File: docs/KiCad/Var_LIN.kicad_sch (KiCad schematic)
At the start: 28 parts, among them J3 Conn_01x04_Pin, J4 Conn_01x04_Pin, U4 TGS_2611-E00, U5 TLIN2029ADRBRQ1, U6 LMR50410, U7 ATtiny412-SS, U8 BTS4142N

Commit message: Исправление эл.схемы
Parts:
- removed D8: BAV70, Package_TO_SOT_SMD:SOT-23, symbol Diode:BAV70
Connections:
- net OUT1 is gone; now on net OUT: J4.4 (Pin_4)
- net OUT2 is gone; now on net LIN: J4.3 (Pin_3)
- net +5v: now also J3.2 (Pin_2)
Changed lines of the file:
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@@
 	)
 	(junction
-		(at 252.73 50.8)
-		(diameter 0)
-		(color 0 0 0 0)
-	)
-	(junction
 		(at 111.76 142.24)
 		(diameter 0)
@@
 	(wire
 		(pts
-			(xy 238.76 50.8) (xy 242.57 50.8)
-		)
-		(stroke
-			(width 0)
-			(type default)
-		)
-	)
-	(wire
-		(pts
 			(xy 231.14 115.57) (xy 231.14 135.89)
 		)
@@
 	(wire
 		(pts
-			(xy 252.73 50.8) (xy 273.05 50.8)
+			(xy 262.89 50.8) (xy 273.05 50.8)
 		)
 		(stroke
@@
 	(wire
 		(pts
-			(xy 247.65 58.42) (xy 252.73 58.42)
-		)
-		(stroke
-			(width 0)
-			(type default)
-		)
-	)
-	(wire
-		(pts
 			(xy 64.77 139.7) (xy 54.61 139.7)
 		)
@@
 	(wire
 		(pts
-			(xy 247.65 43.18) (xy 252.73 43.18)
-		)
-		(stroke
-			(width 0)
-			(type default)
-		)
-	)
-	(wire
-		(pts
 			(xy 179.07 133.35) (xy 182.88 133.35)
 		)
@@
 	(wire
 		(pts
-			(xy 252.73 58.42) (xy 252.73 50.8)
-		)
-		(stroke
-			(width 0)
-			(type default)
-		)
-	)
-	(wire
-		(pts
 			(xy 170.18 57.15) (xy 175.26 57.15)
 		)
@@
 	(wire
 		(pts
-			(xy 252.73 43.18) (xy 252.73 50.8)
-		)
-		(stroke
-			(width 0)
-			(type default)
-		)
-	)
-	(wire
-		(pts
 			(xy 81.28 132.08) (xy 92.71 132.08)
 		)
@@
 		)
 	)
-	(label "OUT2"
+	(label "LIN"
 		(at 262.89 68.58 180)
 		(effects
@@
 	)
 	(label "+5v"
-		(at 238.76 50.8 180)
+		(at 262.89 50.8 180)
 		(effects
 			(font
@@
 		)
 	)
-	(label "OUT1"
+	(label "OUT"
 		(at 262.89 66.04 180)
 		(effects
@@
 					(unit 1)
 				)
-			)
-		)
-	)
-	(symbol
-		(lib_id "Diode:BAV70")
-		(at 247.65 50.8 270)
-		(unit 1)
-		(body_style 1)
-		(exclude_from_sim no)
-		(in_bom yes)
-		(on_board yes)
-		(in_pos_files yes)
-		(dnp no)
-		(property "Reference" "D8"
-			(at 245.618 41.402 90)
-			(show_name no)
-			(do_not_autoplace no)
-			(effects
-				(font
-					(size 1.27 1.27)
-				)
-				(justify left)
-			)
-		)
-		(property "Value" "BAV70"
-			(at 249.682 41.402 90)
-			(show_name no)
-			(do_not_autoplace no)
-			(effects
-				(font
-					(size 1.27 1.27)
-				)
-				(justify left)
-			)
-		)
-		(property "Footprint" "Package_TO_SOT_SMD:SOT-23"
-			(at 247.65 50.8 0)
-			(hide yes)
-			(show_name no)
-			(do_not_autoplace no)
-			(effects
-				(font
-					(size 1.27 1.27)
-				)
-			)
-		)
-		(property "Datasheet" "https://assets.nexperia.com/documents/data-sheet/BAV70_SER.pdf"
-			(at 247.65 50.8 0)
-			(hide yes)
-			(show_name no)
-			(do_not_autoplace no)
-			(effects
-				(font
-					(size 1.27 1.27)
-				)
-			)
-		)
-		(property "Description" "Dual 100V 215mA high-speed switching diodes, common cathode, SOT-23"
-			(at 247.65 50.8 0)
-			(hide yes)
-			(show_name no)
-			(do_not_autoplace no)
-			(effects
-				(font
-					(size 1.27 1.27)
-				)
-			)
-		)
-		(pin "2"
-		)
-		(pin "1"
-		)
-		(pin "3"
-		)
-		(instances
-			(project "Датчик утечки газа 2026"
-				(path "/a17a5c65-2c8f-4811-931f-2f1634edc76c/5b8447ab-854c-4557-a5fd-39e271aa8951"
-					(reference "D8")
-					(unit 1)
-				)

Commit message: Корректировать номиналы схемы питания. Uвых=4,7v
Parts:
- R21: value 88k -> 82k
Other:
- note added: "4,7В"
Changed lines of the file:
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@@
+		)
+	)
+	(text "4,7В"
+		(exclude_from_sim no)
+		(at 147.828 120.904 0)
+		(effects
+			(font
+				(size 1.27 1.27)
+			)
 		)
 	)
@@
 			)
 		)
-		(property "Value" "88k"
+		(property "Value" "82k"
 			(at 140.208 127.508 0)
 			(show_name no)

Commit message: Разделить платы разных версий
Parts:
- removed D4: BAV70, Package_TO_SOT_SMD:SOT-23, symbol Diode:BAV70
- added D8: MBRA360, Diode_SMD:D_SMA, symbol Device:D
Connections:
- net +24V: now also D8.2 (A); no longer U8.4 (Vbb)
- net +24_V: now reaches R17.2
- net +24_V: now also U8.4 (Vbb), D8.1 (K)
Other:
- moved on the sheet: J3, J4

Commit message: Исправление разводки платы Ver_LIN
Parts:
- R17: footprint Resistor_SMD:R_1210_3225Metric_Pad1.30x2.65mm_HandSolder -> Resistor_SMD:R_1206_3216Metric
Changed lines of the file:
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@@
 			)
 		)
-		(property "Footprint" "Resistor_SMD:R_1210_3225Metric_Pad1.30x2.65mm_HandSolder"
+		(property "Footprint" "Resistor_SMD:R_1206_3216Metric"
 			(at 74.93 130.302 90)
 			(hide yes)

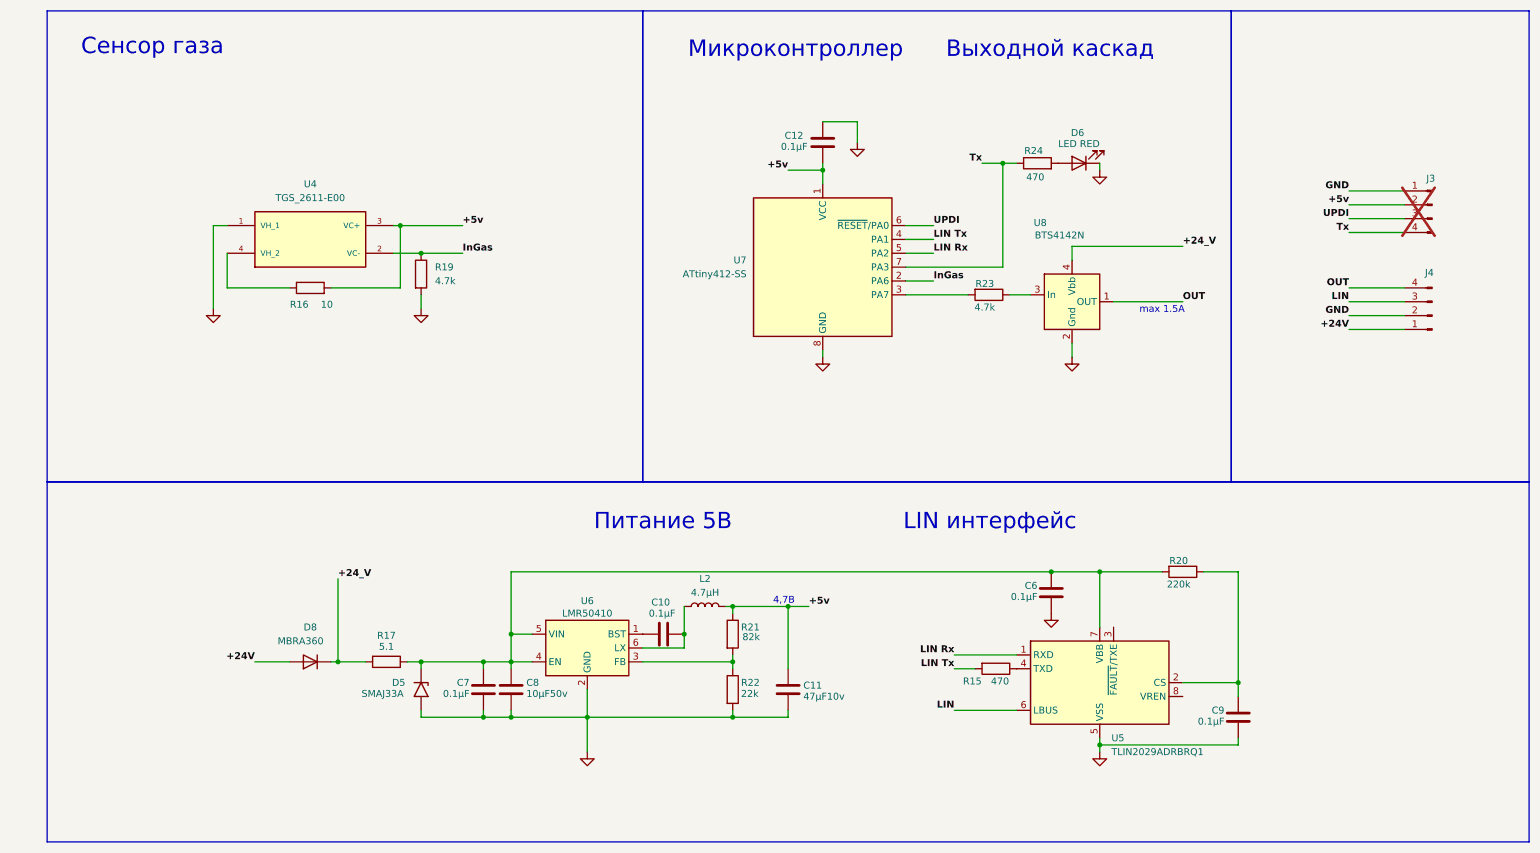
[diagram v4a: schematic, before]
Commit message: Изменить выходной ключ на умный. Правки печатной платы
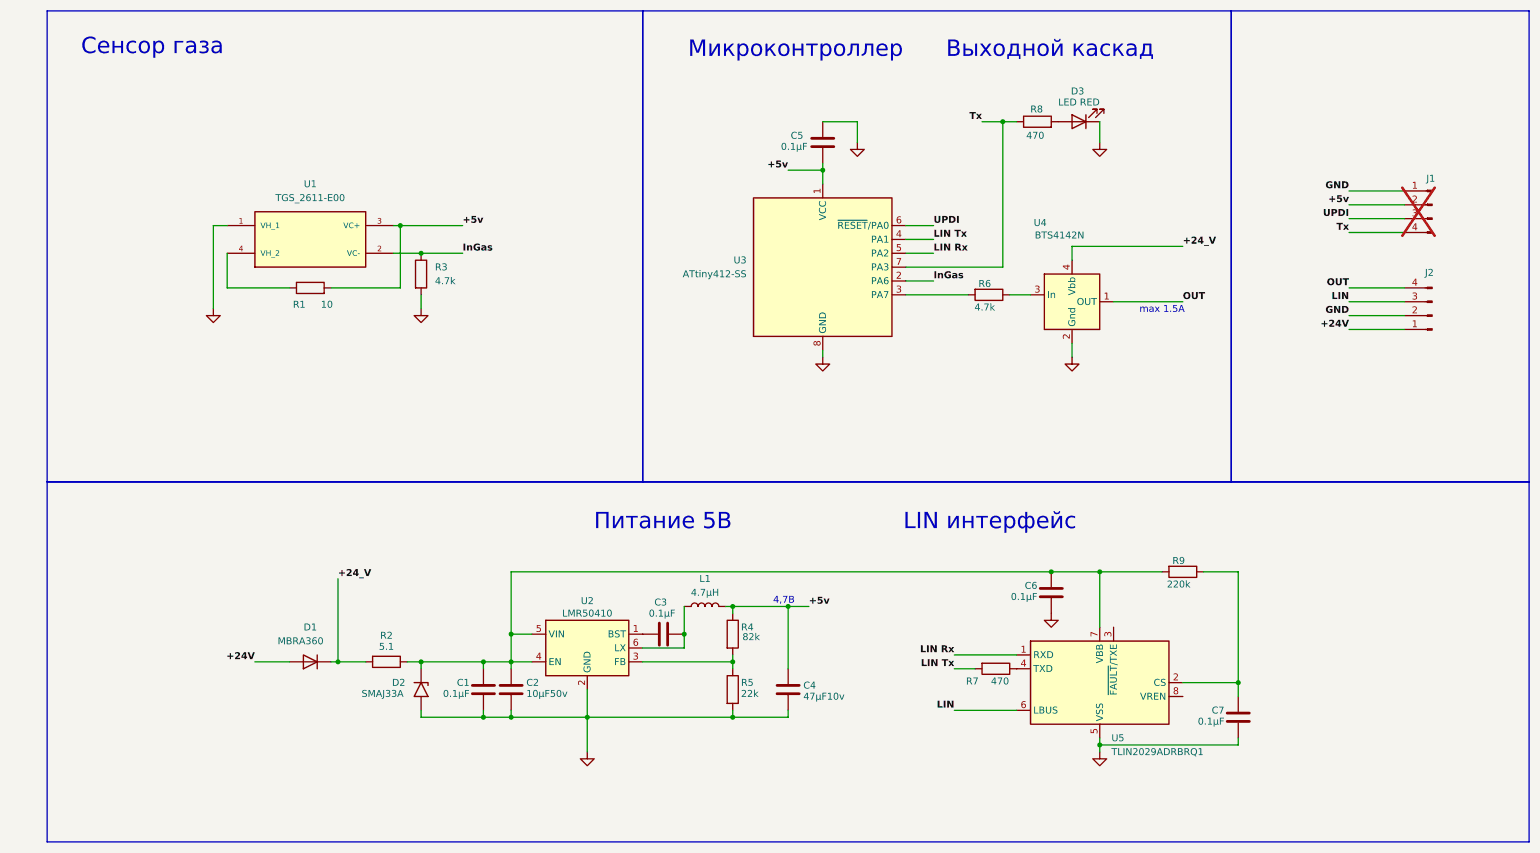
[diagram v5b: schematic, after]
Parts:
- J2: renamed from J4; footprint Connector_Pin:AMP SEAL 3.00mm_4p -> Connector_DIN:SSEAL_4
- U1: renamed from U4; footprint Sensor:TO180P920X780-4P -> Sensor_Humidity:TO180P920X780-4P
- renumbered C7 to C1, C8 to C2, C10 to C3, C11 to C4, C12 to C5, C9 to C7, D8 to D1, D5 to D2, D6 to D3, J3 to J1, L2 to L1, R16 to R1, R17 to R2, R19 to R3, R21 to R4, R22 to R5, R23 to R6, R15 to R7, R24 to R8, R20 to R9, U6 to U2, U7 to U3, U8 to U4
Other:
- moved on the sheet: D3, R8

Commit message: Коррекция ПП. Замена выходной ключ на BTS72002
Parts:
- R2: footprint Resistor_SMD:R_1206_3216Metric -> Resistor_SMD:R_0805_2012Metric
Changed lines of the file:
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@@
 			)
 		)
-		(property "Footprint" "Resistor_SMD:R_1206_3216Metric"
+		(property "Footprint" "Resistor_SMD:R_0805_2012Metric"
 			(at 74.93 130.302 90)
 			(hide yes)

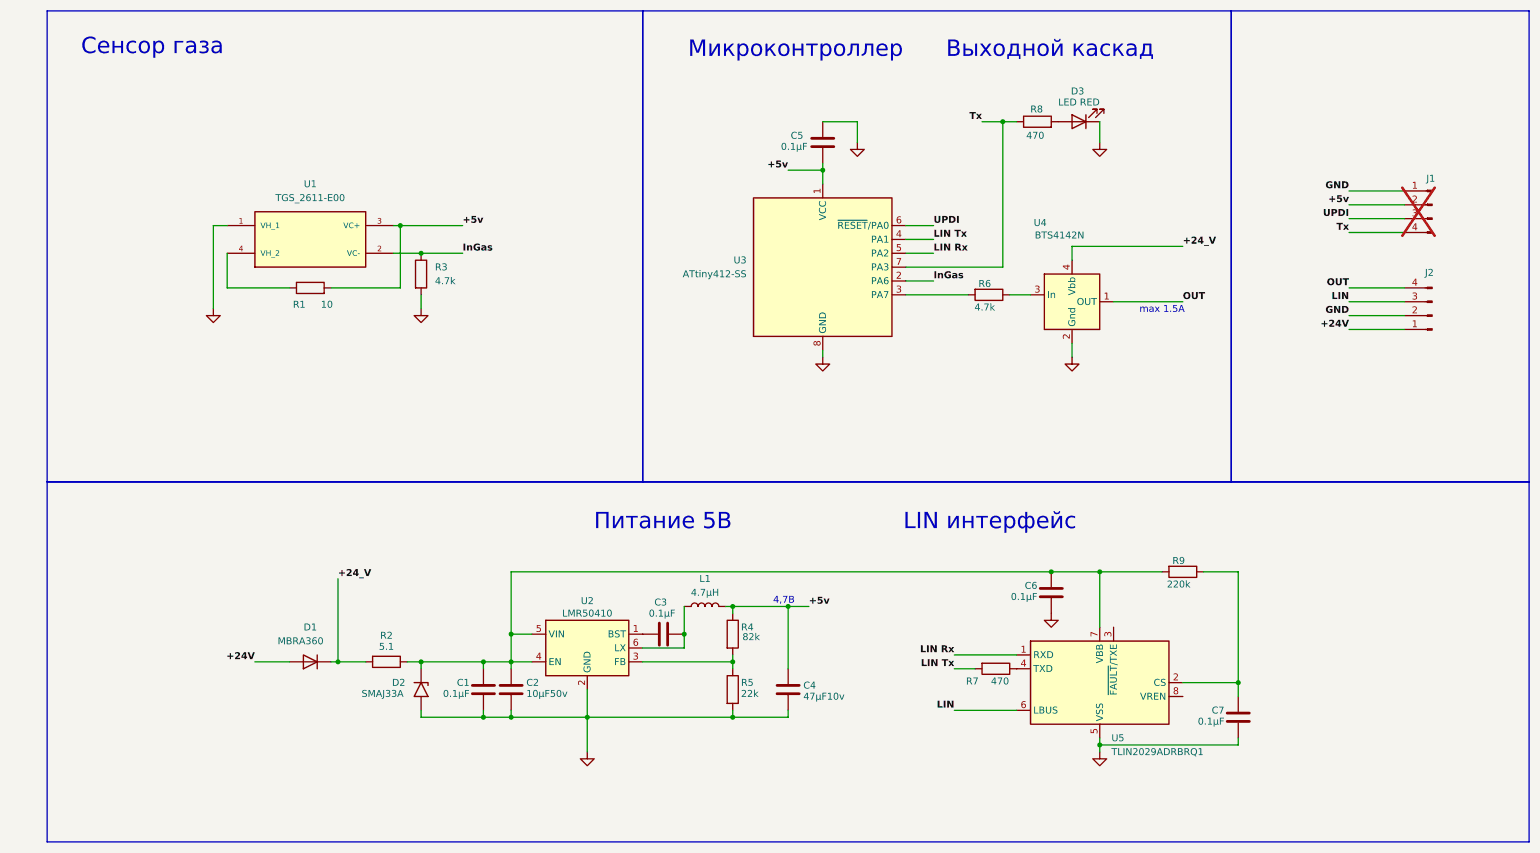
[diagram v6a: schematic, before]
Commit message: Обновить схемы и логику выходного ключа
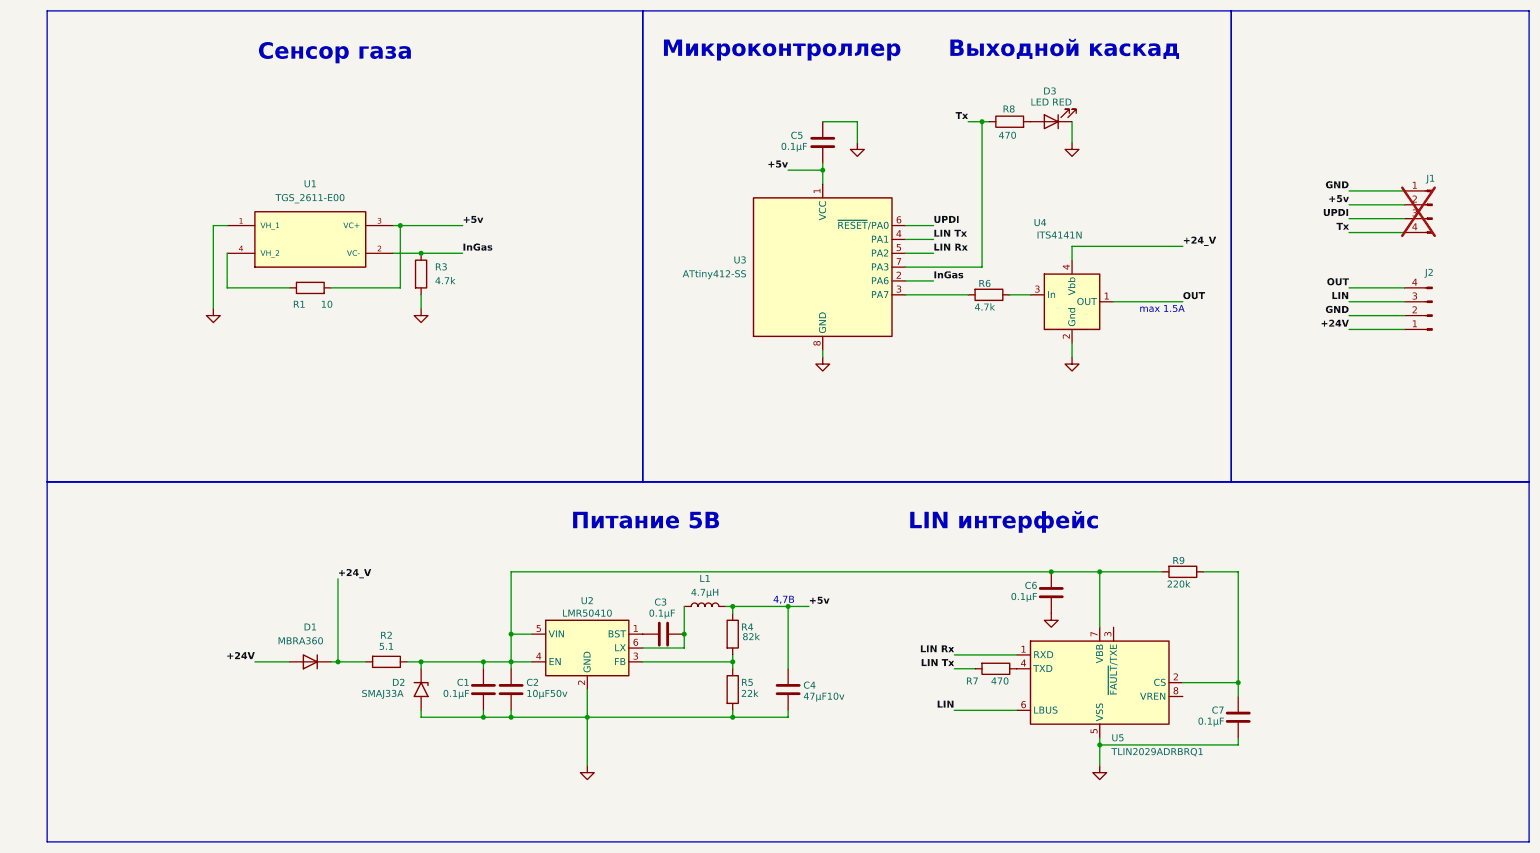
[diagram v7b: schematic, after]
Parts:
- U4: value BTS4142N -> ITS4141N
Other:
- moved on the sheet: D3, R8
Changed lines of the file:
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@@
 	(text "Сенсор газа"
 		(exclude_from_sim no)
-		(at 32.004 19.304 0)
+		(at 65.532 20.32 0)
 		(effects
 			(font
 				(size 3 3)
+				(thickness 0.6)
+				(bold yes)
 			)
 		)
@@
 			(font
 				(size 3 3)
+				(thickness 0.6)
+				(bold yes)
 			)
 		)
@@
 			(font
 				(size 3 3)
+				(thickness 0.6)
+				(bold yes)
 			)
 		)
@@
 	)
 	(junction
-		(at 205.74 147.32)
-		(diameter 0)
-		(color 0 0 0 0)
-	)
-	(junction
 		(at 97.79 142.24)
 		(diameter 0)
@@
 	)
 	(junction
-		(at 187.96 33.02)
-		(diameter 0)
-		(color 0 0 0 0)
-	)
-	(junction
 		(at 154.94 41.91)
 		(diameter 0)
@@
 	)
 	(junction
+		(at 184.15 33.02)
+		(diameter 0)
+		(color 0 0 0 0)
+	)
+	(junction
 		(at 66.04 132.08)
 		(diameter 0)
@@
 	)
 	(junction
+		(at 205.74 147.32)
+		(diameter 0)
+		(color 0 0 0 0)
+	)
+	(junction
 		(at 129.54 127)
 		(diameter 0)
@@
 	(wire
 		(pts
-			(xy 205.74 147.32) (xy 205.74 148.59)
+			(xy 205.74 147.32) (xy 205.74 151.13)
 		)
 		(stroke
@@
 	(wire
 		(pts
-			(xy 187.96 33.02) (xy 190.5 33.02)
-		)
-		(stroke
-			(width 0)
-			(type default)
-		)
-	)
-	(wire
-		(pts
 			(xy 148.59 140.97) (xy 148.59 142.24)
 		)
@@
 	(wire
 		(pts
-			(xy 111.76 148.59) (xy 111.76 142.24)
+			(xy 111.76 151.13) (xy 111.76 142.24)
 		)
 		(stroke
@@
 	(wire
 		(pts
+			(xy 184.15 33.02) (xy 185.42 33.02)
+		)
+		(stroke
+			(width 0)
+			(type default)
+		)
+	)
+	(wire
+		(pts
 			(xy 148.59 133.35) (xy 148.59 121.92)
 		)
@@
 	(wire
 		(pts
-			(xy 187.96 33.02) (xy 187.96 59.69)
+			(xy 184.15 33.02) (xy 184.15 59.69)
 		)
 		(stroke
@@
 	(wire
 		(pts
-			(xy 184.15 33.02) (xy 187.96 33.02)
+			(xy 181.61 33.02) (xy 184.15 33.02)
 		)
 		(stroke
@@
 	(wire
 		(pts
-			(xy 170.18 59.69) (xy 187.96 59.69)
+			(xy 170.18 59.69) (xy 184.15 59.69)
 		)
 		(stroke
@@
 	(wire
 		(pts
-			(xy 205.74 36.83) (xy 205.74 33.02)
+			(xy 200.66 36.83) (xy 200.66 33.02)
 		)
 		(stroke
@@
 	)
 	(label "Tx"
-		(at 184.15 33.02 180)
+		(at 181.61 33.02 180)
 		(effects
 			(font
@@
 	(symbol
 		(lib_id "power:GND")
-		(at 205.74 36.83 0)
+		(at 200.66 36.83 0)
 		(unit 1)
 		(body_style 1)
@@
 		(fields_autoplaced yes)
 		(property "Reference" "#PWR08"
-			(at 205.74 43.18 0)
+			(at 200.66 43.18 0)
 			(hide yes)
 			(show_name no)
@@
 		)
 		(property "Value" "GND"
-			(at 205.74 41.91 0)
+			(at 200.66 41.91 0)
 			(hide yes)
 			(show_name no)
@@
 		)
 		(property "Footprint" ""
-			(at 205.74 36.83 0)
+			(at 200.66 36.83 0)
 			(hide yes)
 			(show_name no)
@@
 		)
 		(property "Datasheet" ""
-			(at 205.74 36.83 0)
+			(at 200.66 36.83 0)
 			(hide yes)
 			(show_name no)
@@
 		)
 		(property "Description" "Power symbol creates a global label with name \"GND\" , ground"
-			(at 205.74 36.83 0)
+			(at 200.66 36.83 0)
 			(hide yes)
 			(show_name no)
@@
 	(symbol
 		(lib_id "power:GND")
-		(at 205.74 148.59 0)
+		(at 205.74 151.13 0)
 		(unit 1)
 		(body_style 1)
@@
 		(fields_autoplaced yes)
 		(property "Reference" "#PWR09"
-			(at 205.74 154.94 0)
+			(at 205.74 157.48 0)
 			(hide yes)
 			(show_name no)
@@
 		)
 		(property "Value" "GND"
-			(at 205.74 153.67 0)
+			(at 205.74 156.21 0)
 			(hide yes)
 			(show_name no)
@@
 		)
 		(property "Footprint" ""
-			(at 205.74 148.59 0)
+			(at 205.74 151.13 0)
 			(hide yes)
 			(show_name no)
@@
 		)
 		(property "Datasheet" ""
-			(at 205.74 148.59 0)
+			(at 205.74 151.13 0)
 			(hide yes)
 			(show_name no)
@@
 		)
 		(property "Description" "Power symbol creates a global label with name \"GND\" , ground"
-			(at 205.74 148.59 0)
+			(at 205.74 151.13 0)
 			(hide yes)
 			(show_name no)
@@
 	(symbol
 		(lib_id "Device:LED")
-		(at 201.93 33.02 180)
+		(at 196.85 33.02 180)
 		(unit 1)
 		(body_style 1)
@@
 		(dnp no)
 		(property "Reference" "D3"
-			(at 201.676 27.432 0)
+			(at 196.596 27.432 0)
 			(show_name no)
 			(do_not_autoplace no)
@@
 		)
 		(property "Value" "LED RED"
-			(at 201.93 29.464 0)
+			(at 196.85 29.464 0)
 			(show_name no)
 			(do_not_autoplace no)
@@
 		)
 		(property "Footprint" "LED_SMD:LED_0805_2012Metric"
-			(at 201.93 33.02 0)
+			(at 196.85 33.02 0)
 			(hide yes)
 			(show_name no)
@@
 		)
 		(property "Datasheet" ""
-			(at 201.93 33.02 0)
+			(at 196.85 33.02 0)
 			(hide yes)
 			(show_name no)
@@
 		)
 		(property "Description" "FYLS-0805URC"
-			(at 201.93 33.02 0)
+			(at 196.85 33.02 0)
 			(hide yes)
 			(show_name no)
@@
 		)
 		(property "Sim.Pins" "1=K 2=A"
-			(at 201.93 33.02 0)
+			(at 196.85 33.02 0)
 			(hide yes)
 			(show_name no)
@@
 	(symbol
 		(lib_id "Device:R")
-		(at 194.31 33.02 90)
+		(at 189.23 33.02 90)
 		(unit 1)
 		(body_style 1)
@@
 		(dnp no)
 		(property "Reference" "R8"
-			(at 195.326 30.734 90)
+			(at 190.246 30.734 90)
 			(show_name no)
 			(do_not_autoplace no)
@@
 		)
 		(property "Value" "470"
-			(at 195.58 35.56 90)
+			(at 190.5 35.56 90)
 			(show_name no)
 			(do_not_autoplace no)
@@
 		)
 		(property "Footprint" "Resistor_SMD:R_0603_1608Metric"
-			(at 194.31 34.798 90)
+			(at 189.23 34.798 90)
 			(hide yes)
 			(show_name no)
@@
 		)
 		(property "Datasheet" ""
-			(at 194.31 33.02 0)
+			(at 189.23 33.02 0)
 			(hide yes)
 			(show_name no)
@@
 		)
 		(property "Description" "Resistor"
-			(at 194.31 33.02 0)
+			(at 189.23 33.02 0)
 			(hide yes)
 			(show_name no)
@@
 			)
 		)
-		(property "Value" "BTS4142N"
+		(property "Value" "ITS4141N"
 			(at 198.374 53.848 0)
 			(show_name no)
@@
 	(symbol
 		(lib_id "power:GND")
-		(at 111.76 148.59 0)
+		(at 111.76 151.13 0)
 		(unit 1)
 		(body_style 1)
@@
 		(fields_autoplaced yes)
 		(property "Reference" "#PWR03"
-			(at 111.76 154.94 0)
+			(at 111.76 157.48 0)
 			(hide yes)
 			(show_name no)
@@
 		)
 		(property "Value" "GND"
-			(at 111.76 153.67 0)
+			(at 111.76 156.21 0)
 			(hide yes)
 			(show_name no)
@@
 		)
 		(property "Footprint" ""
-			(at 111.76 148.59 0)
+			(at 111.76 151.13 0)
 			(hide yes)
 			(show_name no)
@@
 		)
 		(property "Datasheet" ""
-			(at 111.76 148.59 0)
+			(at 111.76 151.13 0)
 			(hide yes)
 			(show_name no)
@@
 		)
 		(property "Description" "Power symbol creates a global label with name \"GND\" , ground"
-			(at 111.76 148.59 0)
+			(at 111.76 151.13 0)
 			(hide yes)
 			(show_name no)
